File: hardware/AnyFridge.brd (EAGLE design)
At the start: 83.5 x 69.8 mm, 11 parts

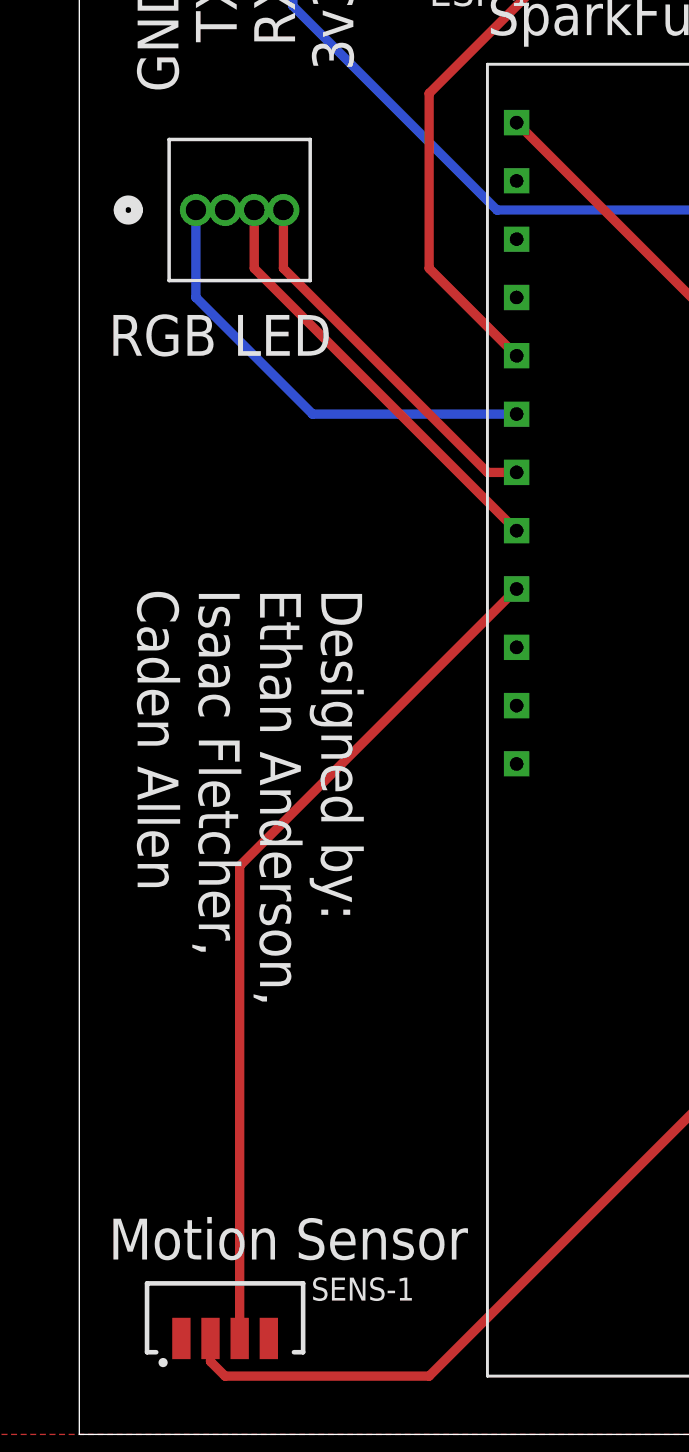
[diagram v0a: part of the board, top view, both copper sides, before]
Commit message: attempted fix for LED spacing
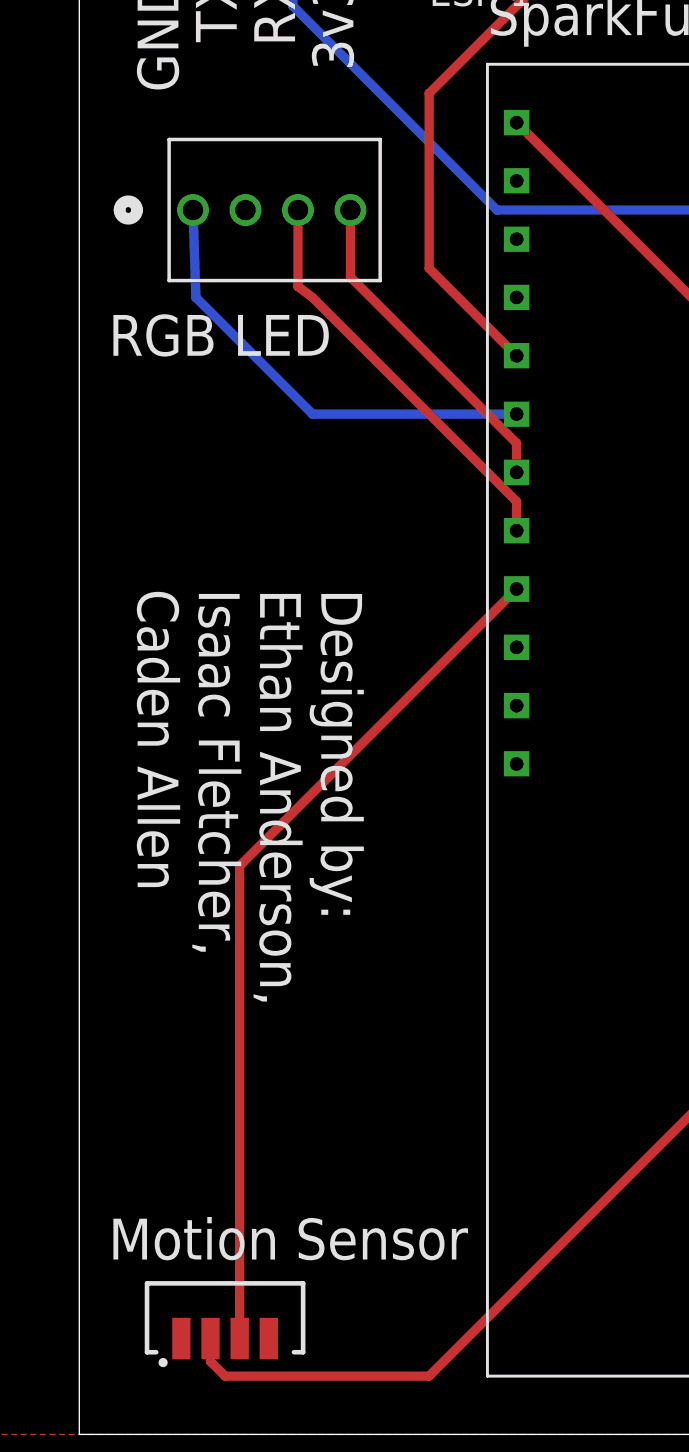
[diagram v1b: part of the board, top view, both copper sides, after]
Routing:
- net GREEN: track 16.4 -> 14.4 mm
- net BLUE: track 18.7 -> 18.0 mm
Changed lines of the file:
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@@
 <grid distance="50" unitdist="mil" unit="mil" style="lines" multiple="1" display="no" altdistance="5" altunitdist="mil" altunit="mil"/>
 <layers>
-<layer number="1" name="Top" color="4" fill="1" visible="no" active="yes"/>
+<layer number="1" name="Top" color="4" fill="1" visible="yes" active="yes"/>
 <layer number="2" name="Route2" color="1" fill="3" visible="no" active="no"/>
 <layer number="3" name="Route3" color="4" fill="3" visible="no" active="no"/>
@@
 <attribute name="MF" value="Vishay" x="35.56" y="-148.59" size="1.778" layer="27" display="off"/>
 <attribute name="MP" value="TSSP77038TT" x="35.56" y="-148.59" size="1.778" layer="27" display="off"/>
+<attribute name="NAME" x="12.64" y="5.83" size="1" layer="25" ratio="20" rot="SR0"/>
 <attribute name="NAME" x="12.64" y="5.83" size="1" layer="51" ratio="21" rot="SR0"/>
-<attribute name="NAME" x="12.64" y="5.83" size="1" layer="25" ratio="20" rot="SR0"/>
 <attribute name="PACKAGE" value="None" x="35.56" y="-148.59" size="1.778" layer="27" display="off"/>
 <attribute name="PRICE" value="None" x="35.56" y="-148.59" size="1.778" layer="27" display="off"/>
@@
 </polygon>
 <contactref element="TP_GND" pad="TP"/>
+<wire x1="49.53" y1="40.64" x2="58.42" y2="55.88" width="0" layer="19" extent="1-1"/>
+<wire x1="41.91" y1="26.67" x2="49.53" y2="40.64" width="0" layer="19" extent="1-1"/>
+<wire x1="10.795" y1="4.18" x2="41.91" y2="26.67" width="0" layer="19" extent="1-1"/>
+<wire x1="6.985" y1="4.18" x2="10.795" y2="4.18" width="0" layer="19" extent="1-1"/>
+<wire x1="9.779" y1="53.34" x2="49.53" y2="40.64" width="0" layer="19" extent="1-1"/>
+<wire x1="6.35" y1="66.04" x2="9.779" y2="53.34" width="0" layer="19" extent="1-1"/>
 </signal>
 <signal name="3.3V">
@@
 <contactref element="LED-1" pad="1"/>
 <contactref element="ESP-1" pad="33"/>
-<wire x1="7.62" y1="53.34" x2="7.62" y2="49.53" width="0.4064" layer="16"/>
+<wire x1="7.493" y1="53.34" x2="7.62" y2="49.53" width="0.4064" layer="16"/>
 <wire x1="21.59" y1="44.45" x2="12.7" y2="44.45" width="0.4064" layer="16"/>
 <wire x1="7.62" y1="49.53" x2="12.7" y2="44.45" width="0.4064" layer="16"/>
@@
 <contactref element="LED-1" pad="3"/>
 <contactref element="ESP-1" pad="12"/>
-<wire x1="21.59" y1="39.37" x2="10.16" y2="50.8" width="0.4064" layer="1"/>
-<wire x1="10.16" y1="53.34" x2="10.16" y2="50.8" width="0.4064" layer="1"/>
+<wire x1="21.59" y1="39.37" x2="21.59" y2="40.64" width="0.4064" layer="1"/>
+<wire x1="21.59" y1="40.64" x2="12.7" y2="49.53" width="0.4064" layer="1"/>
+<wire x1="12.7" y1="49.53" x2="12.065" y2="50.00625" width="0.4064" layer="1"/>
+<wire x1="12.065" y1="53.34" x2="12.065" y2="50.00625" width="0.4064" layer="1"/>
 </signal>
 <signal name="GREEN">
 <contactref element="LED-1" pad="4"/>
 <contactref element="ESP-1" pad="27"/>
-<wire x1="21.59" y1="41.91" x2="20.32" y2="41.91" width="0.4064" layer="1"/>
-<wire x1="20.32" y1="41.91" x2="11.43" y2="50.8" width="0.4064" layer="1"/>
-<wire x1="11.43" y1="50.8" x2="11.43" y2="53.34" width="0.4064" layer="1"/>
+<wire x1="21.59" y1="41.91" x2="21.59" y2="43.18" width="0.4064" layer="1"/>
+<wire x1="21.59" y1="43.18" x2="14.351" y2="50.419" width="0.4064" layer="1"/>
+<wire x1="14.351" y1="50.419" x2="14.351" y2="53.34" width="0.4064" layer="1"/>
 </signal>
 <signal name="N$1">

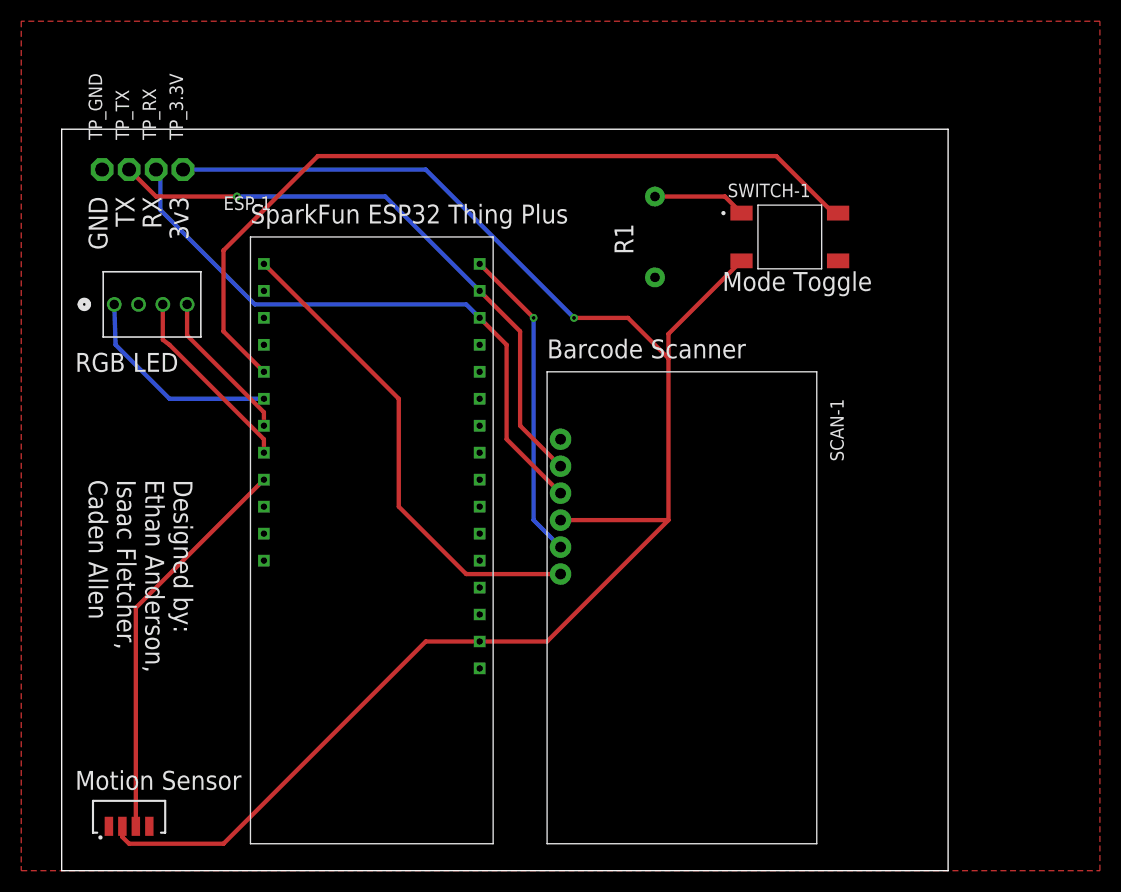
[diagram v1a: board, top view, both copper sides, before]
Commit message: Updated board and schematic to use appropriate ESP library
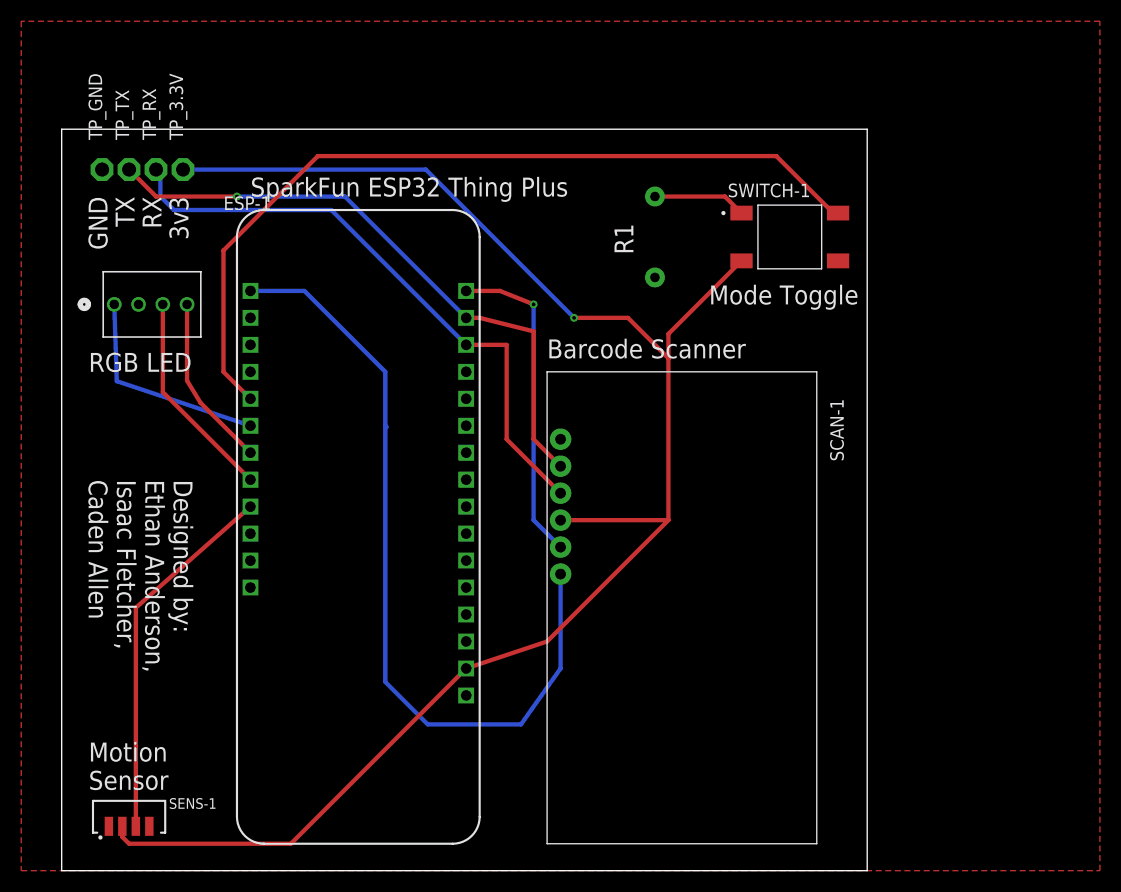
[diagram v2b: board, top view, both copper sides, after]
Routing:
- net STAT: track 46.0 -> 75.0 mm
- net SENS-OUT: track 37.6 -> 35.0 mm
- net SWI-OUT: track 76.8 -> 78.8 mm
- net BLUE: track 18.0 -> 19.9 mm
- net GREEN: track 14.4 -> 16.3 mm
- net RX1: track 57.9 -> 57.2 mm
- net TRIG: track 29.8 -> 30.5 mm
- net 3.3V: track 155.8 -> 155.2 mm
- net RED: track 19.9 -> 20.5 mm
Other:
- board size 83.5 x 69.8 mm -> 75.9 x 69.8 mm

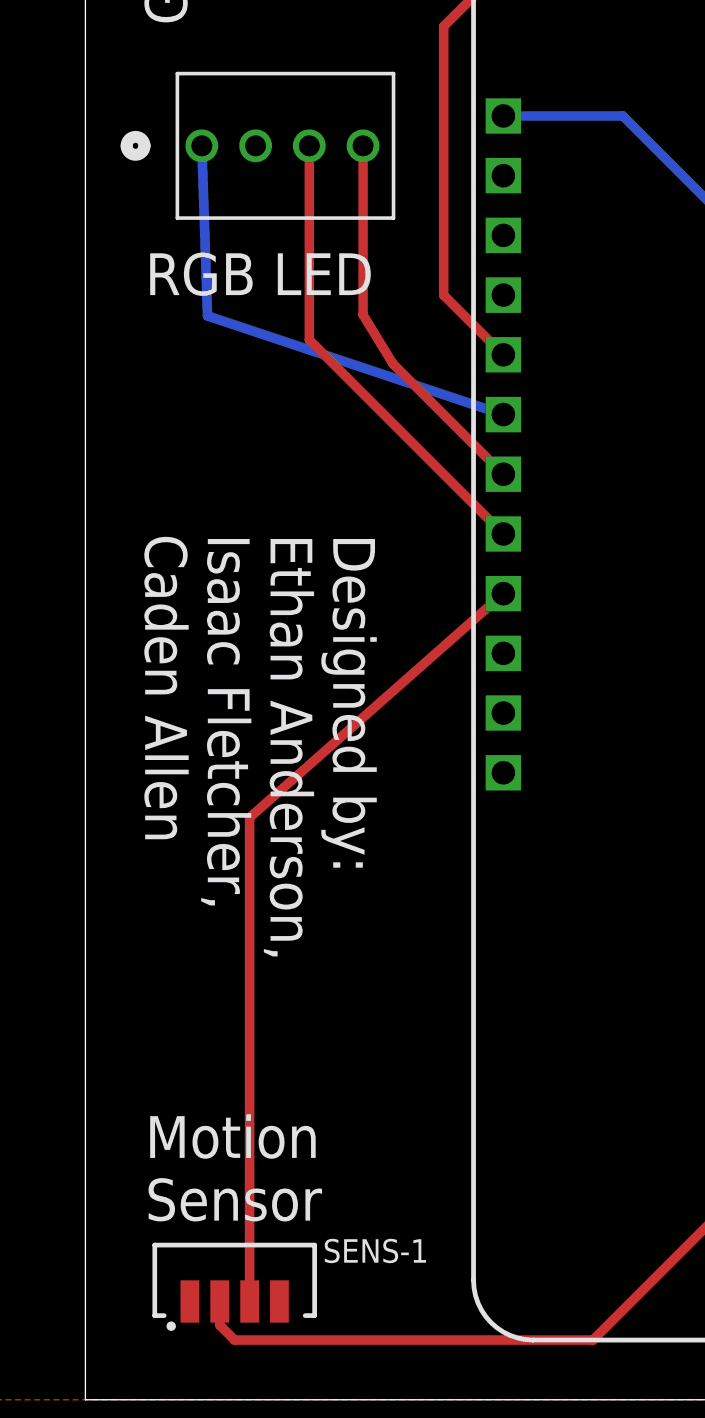
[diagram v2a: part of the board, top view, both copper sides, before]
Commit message: Make traces to LED less wonky
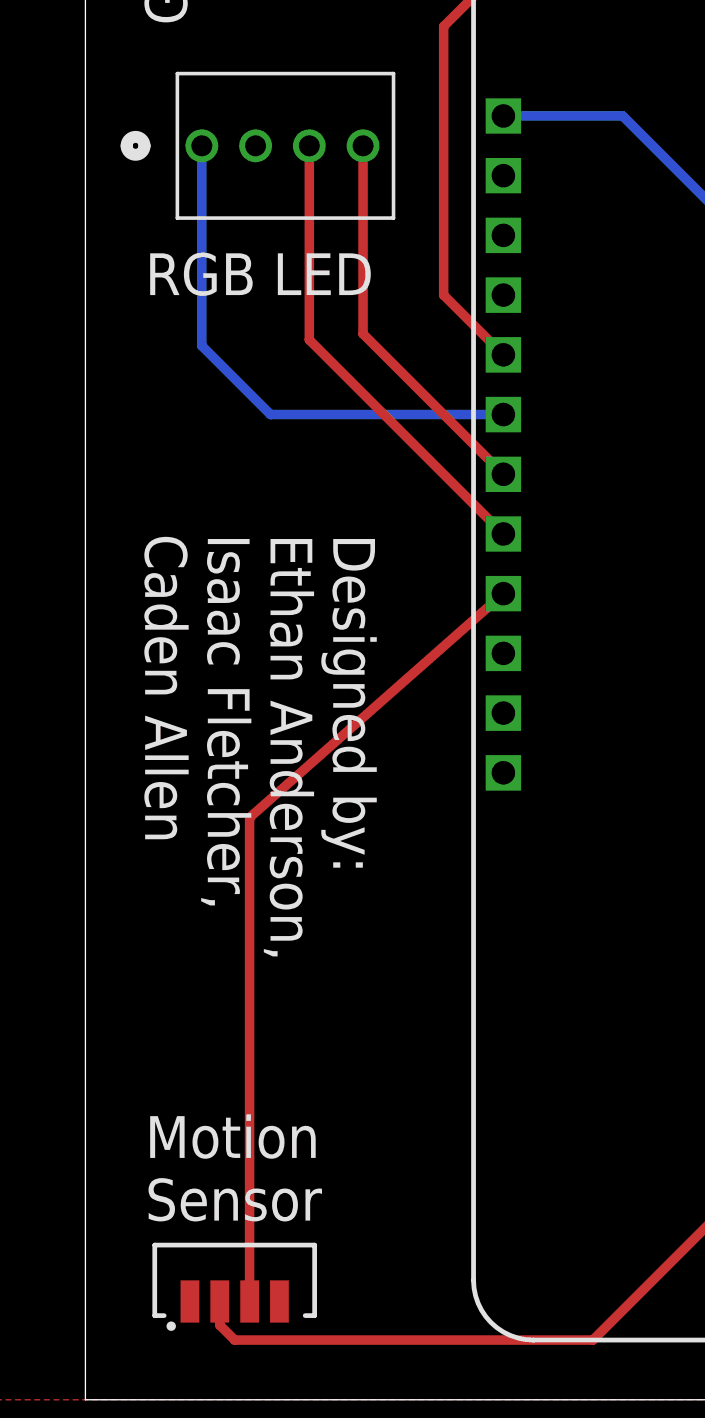
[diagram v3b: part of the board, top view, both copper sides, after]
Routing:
- net RED: track 20.5 -> 22.5 mm
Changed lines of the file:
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@@
 <setting verticaltext="up"/>
 </settings>
-<grid distance="50" unitdist="mil" unit="mil" style="lines" multiple="1" display="no" altdistance="5" altunitdist="mil" altunit="mil"/>
+<grid distance="0.05" unitdist="inch" unit="inch" style="lines" multiple="1" display="no" altdistance="5" altunitdist="mil" altunit="mil"/>
 <layers>
 <layer number="1" name="Top" color="4" fill="1" visible="yes" active="yes"/>
@@
 <attribute name="MF" value="Vishay" x="35.56" y="-148.59" size="1.778" layer="27" display="off"/>
 <attribute name="MP" value="TSSP77038TT" x="35.56" y="-148.59" size="1.778" layer="27" display="off"/>
+<attribute name="NAME" x="12.64" y="5.83" size="1" layer="25" ratio="20" rot="SR0"/>
 <attribute name="NAME" x="12.64" y="5.83" size="1" layer="51" ratio="21" rot="SR0"/>
-<attribute name="NAME" x="12.64" y="5.83" size="1" layer="25" ratio="20" rot="SR0"/>
 <attribute name="PACKAGE" value="None" x="35.56" y="-148.59" size="1.778" layer="27" display="off"/>
 <attribute name="PRICE" value="None" x="35.56" y="-148.59" size="1.778" layer="27" display="off"/>
@@
 <contactref element="LED-1" pad="1"/>
 <contactref element="ESP-1" pad="33"/>
-<wire x1="7.493" y1="53.34" x2="7.73415625" y2="46.10528125" width="0.4064" layer="16"/>
-<wire x1="20.32" y1="41.91" x2="7.73415625" y2="46.10528125" width="0.4064" layer="16"/>
+<wire x1="10.414" y1="41.91" x2="20.32" y2="41.91" width="0.4064" layer="16"/>
+<wire x1="7.493" y1="44.831" x2="10.414" y2="41.91" width="0.4064" layer="16"/>
+<wire x1="7.493" y1="53.34" x2="7.493" y2="44.831" width="0.4064" layer="16"/>
 </signal>
 <signal name="BLUE">
 <contactref element="LED-1" pad="3"/>
 <contactref element="ESP-1" pad="12"/>
-<wire x1="20.32" y1="36.83" x2="12.065" y2="45.085" width="0.4064" layer="1"/>
 <wire x1="12.065" y1="53.34" x2="12.065" y2="45.085" width="0.4064" layer="1"/>
+<wire x1="12.065" y1="45.085" x2="20.32" y2="36.83" width="0.4064" layer="1"/>
 </signal>
 <signal name="GREEN">
 <contactref element="LED-1" pad="4"/>
 <contactref element="ESP-1" pad="27"/>
-<wire x1="20.32" y1="39.37" x2="15.621" y2="44.069" width="0.4064" layer="1"/>
-<wire x1="15.621" y1="44.069" x2="14.351" y2="46.1496375" width="0.4064" layer="1"/>
-<wire x1="14.351" y1="46.1496375" x2="14.351" y2="53.34" width="0.4064" layer="1"/>
+<wire x1="14.351" y1="53.34" x2="14.351" y2="45.339" width="0.4064" layer="1"/>
+<wire x1="14.351" y1="45.339" x2="20.32" y2="39.37" width="0.4064" layer="1"/>
 </signal>
 <signal name="N$1">
